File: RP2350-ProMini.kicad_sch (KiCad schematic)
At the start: 44 parts, among them J1 CONN_L, J2 CONN_U, J3 CONN_R2, J4 CONN_R, J5 CONN_R3, J6 USB_B_Micro, J7 CONN_JTAG, Q1 AO3400A, U1 W25Q128JVS, U2 RP2350A-QFN60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

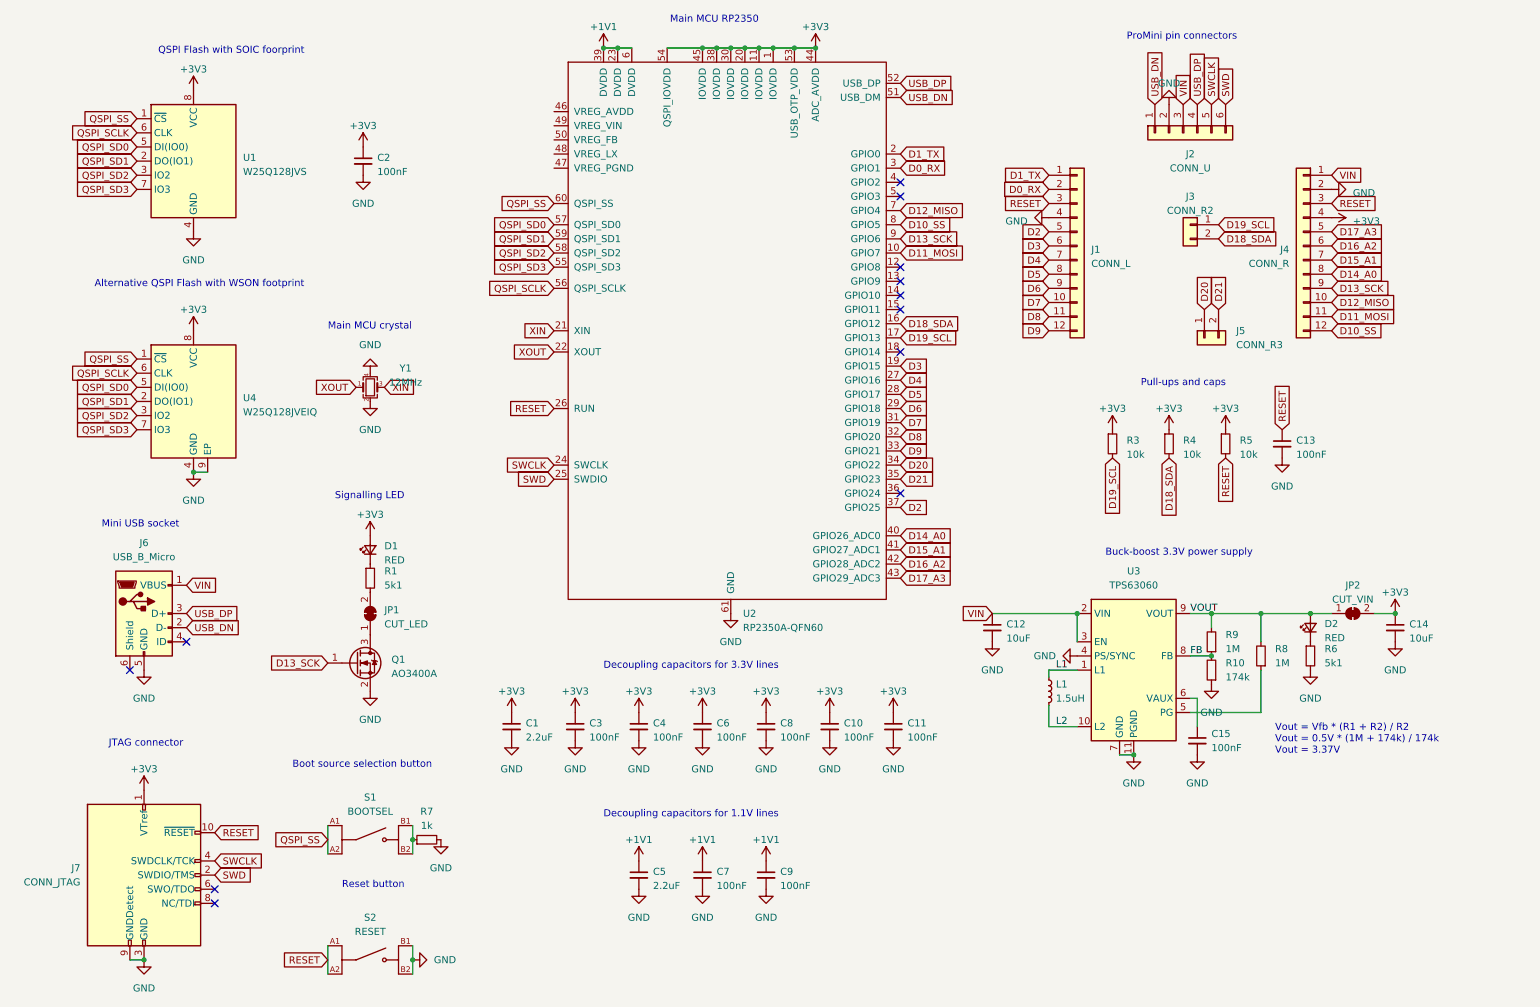
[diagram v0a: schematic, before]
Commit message: Added some routing
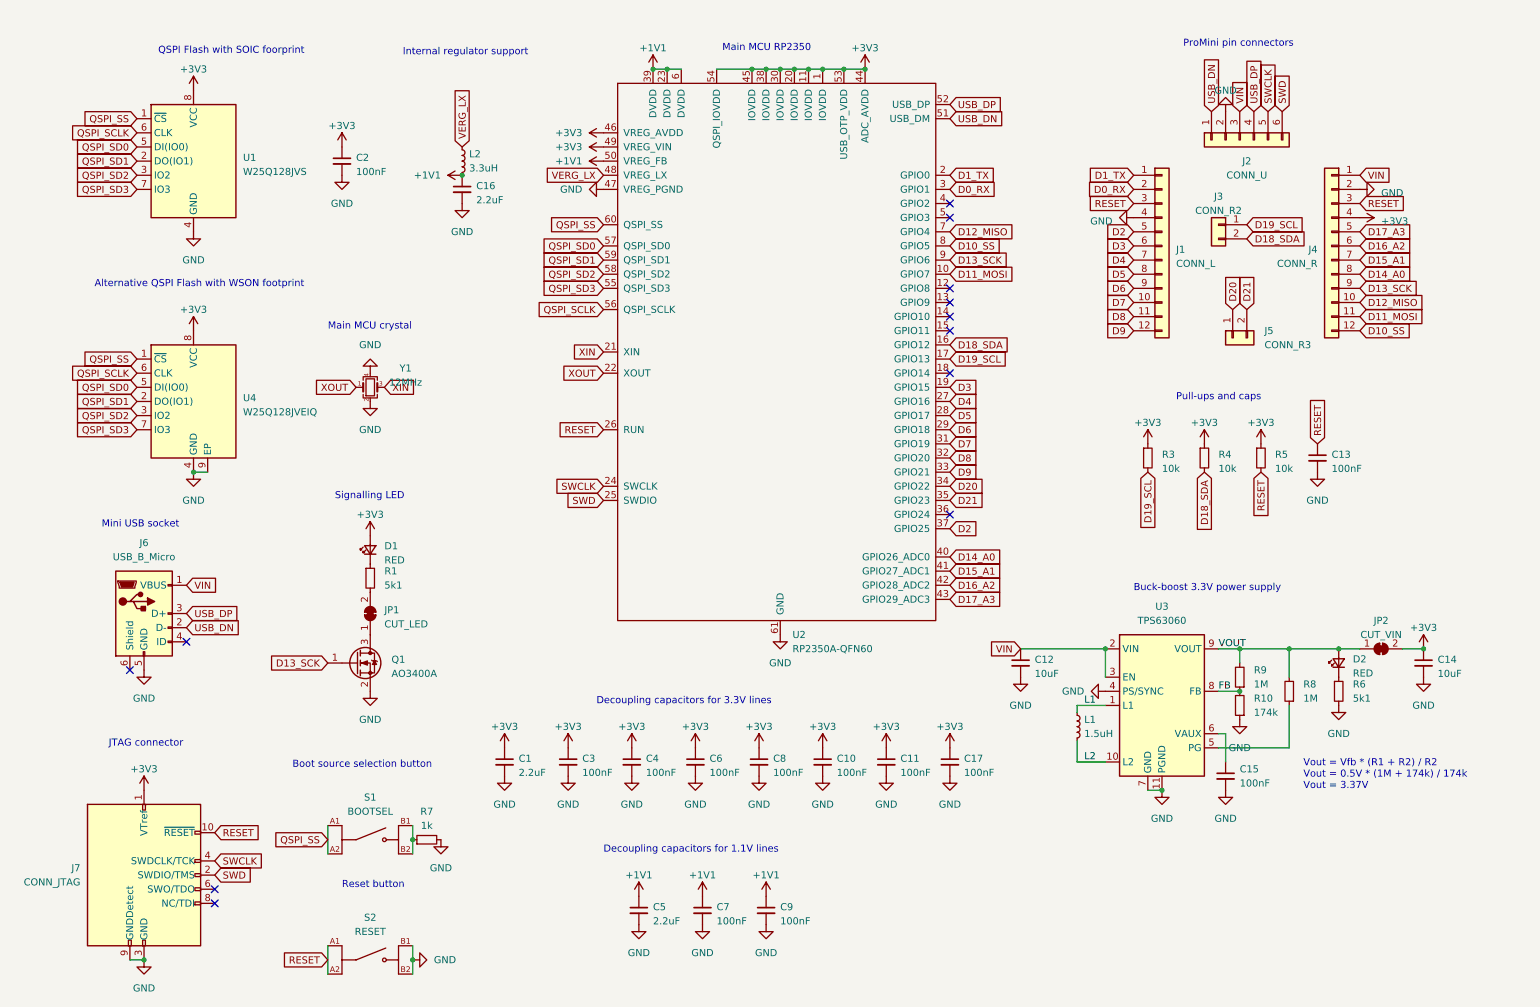
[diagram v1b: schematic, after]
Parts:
- added C16: 2.2uF, Capacitor_SMD:C_0603_1608Metric, symbol Device:C_Small
- added C17: 100nF, Capacitor_SMD:C_0402_1005Metric, symbol Device:C_Small
- added L2: 3.3uH, Inductor_SMD:L_0603_1608Metric, symbol Device:L_Small
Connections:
- net +1V1: now also U2.50 (VREG_FB), C16.1, L2.2
- net +3V3: now also U2.46 (VREG_AVDD), U2.49 (VREG_VIN), C17.1
- net GND: now also U2.47 (VREG_PGND), C16.2, C17.2
- net VERG_LX: now reaches U2.48 (VREG_LX)
- net VERG_LX: now also L2.1
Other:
- note added: "Internal regulator support"
- moved on the sheet: C1, C10, C11, C12, C13, C14, C15, C2, C3, C4, C5, C6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

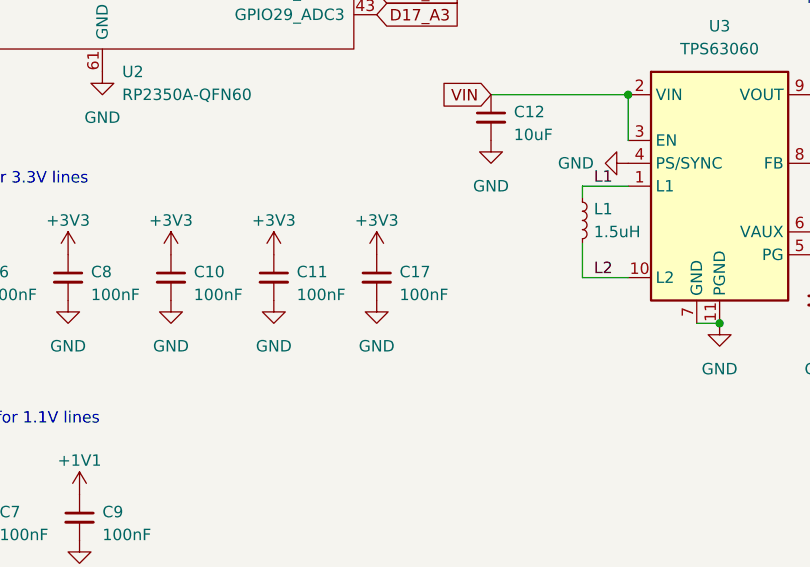
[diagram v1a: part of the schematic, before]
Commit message: Moved staff around.
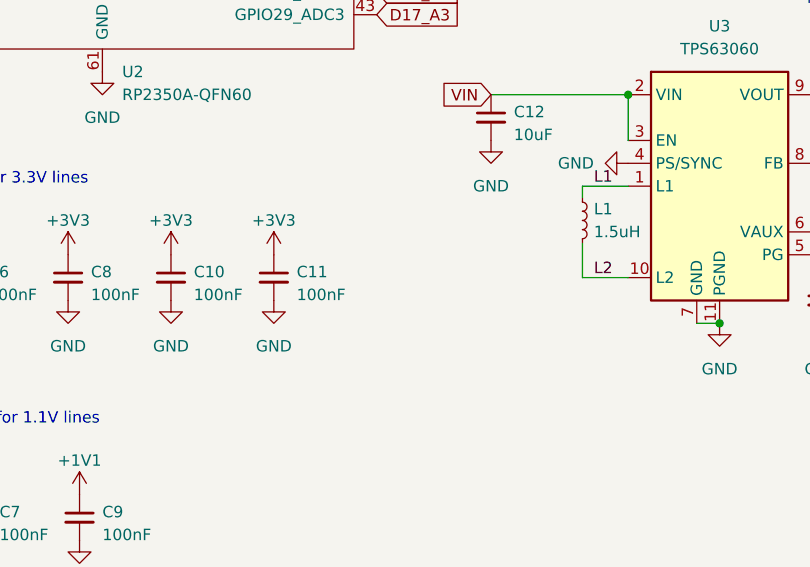
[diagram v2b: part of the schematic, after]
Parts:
- removed C17: 100nF, Capacitor_SMD:C_0402_1005Metric, symbol Device:C_Small
- C1, C16, C5: footprint Capacitor_SMD:C_0603_1608Metric -> Capacitor_SMD:C_0402_1005Metric
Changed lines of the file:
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@@
 	(title_block
 		(title "RP2350-ProMini-0010")
-		(date "2024-09-01")
+		(date "2024-09-03")
 		(rev "1.0")
 		(company "(c) 2024 Andriy Golovnya")
@@
 	)
 	(symbol
-		(lib_id "power:GND")
-		(at 185.42 154.94 0)
-		(unit 1)
-		(exclude_from_sim no)
-		(in_bom yes)
-		(on_board yes)
-		(dnp no)
-		(fields_autoplaced yes)
-		(property "Reference" "#PWR062"
-			(at 185.42 161.29 0)
-			(effects
-				(font
-					(size 1.27 1.27)
-				)
-				(hide yes)
-			)
-		)
-		(property "Value" "GND"
-			(at 185.42 160.02 0)
-			(effects
-				(font
-					(size 1.27 1.27)
-				)
-			)
-		)
-		(property "Footprint" ""
-			(at 185.42 154.94 0)
-			(effects
-				(font
-					(size 1.27 1.27)
-				)
-				(hide yes)
-			)
-		)
-		(property "Datasheet" ""
-			(at 185.42 154.94 0)
-			(effects
-				(font
-					(size 1.27 1.27)
-				)
-				(hide yes)
-			)
-		)
-		(property "Description" ""
-			(at 185.42 154.94 0)
-			(effects
-				(font
-					(size 1.27 1.27)
-				)
-				(hide yes)
-			)
-		)
-		(pin "1"
-		)
-		(instances
-			(project "RP2350-ProMini"
-				(path "/9a38a81c-7302-494f-9784-2ab4342a0a1d"
-					(reference "#PWR062")
-					(unit 1)
-				)
-			)
-		)
-	)
-	(symbol
-		(lib_id "Device:C_Small")
-		(at 185.42 152.4 0)
-		(unit 1)
-		(exclude_from_sim no)
-		(in_bom yes)
-		(on_board yes)
-		(dnp no)
-		(fields_autoplaced yes)
-		(property "Reference" "C17"
-			(at 187.96 151.7713 0)
-			(effects
-				(font
-					(size 1.27 1.27)
-				)
-				(justify left)
-			)
-		)
-		(property "Value" "100nF"
-			(at 187.96 154.3113 0)
-			(effects
-				(font
-					(size 1.27 1.27)
-				)
-				(justify left)
-			)
-		)
-		(property "Footprint" "Capacitor_SMD:C_0402_1005Metric"
-			(at 185.42 152.4 0)
-			(effects
-				(font
-					(size 1.27 1.27)
-				)
-				(hide yes)
-			)
-		)
-		(property "Datasheet" "~"
-			(at 185.42 152.4 0)
-			(effects
-				(font
-					(size 1.27 1.27)
-				)
-				(hide yes)
-			)
-		)
-		(property "Description" ""
-			(at 185.42 152.4 0)
-			(effects
-				(font
-					(size 1.27 1.27)
-				)
-				(hide yes)
-			)
-		)
-		(pin "1"
-		)
-		(pin "2"
-		)
-		(instances
-			(project "RP2350-ProMini"
-				(path "/9a38a81c-7302-494f-9784-2ab4342a0a1d"
-					(reference "C17")
-					(unit 1)
-				)
-			)
-		)
-	)
-	(symbol
 		(lib_id "power:+3V3")
 		(at 173.99 149.86 0)
@@
 	)
 	(symbol
-		(lib_id "power:+3V3")
-		(at 185.42 149.86 0)
-		(unit 1)
-		(exclude_from_sim no)
-		(in_bom yes)
-		(on_board yes)
-		(dnp no)
-		(fields_autoplaced yes)
-		(property "Reference" "#PWR061"
-			(at 185.42 153.67 0)
-			(effects
-				(font
-					(size 1.27 1.27)
-				)
-				(hide yes)
-			)
-		)
-		(property "Value" "+3V3"
-			(at 185.42 146.05 0)
-			(effects
-				(font
-					(size 1.27 1.27)
-				)
-			)
-		)
-		(property "Footprint" ""
-			(at 185.42 149.86 0)
-			(effects
-				(font
-					(size 1.27 1.27)
-				)
-				(hide yes)
-			)
-		)
-		(property "Datasheet" ""
-			(at 185.42 149.86 0)
-			(effects
-				(font
-					(size 1.27 1.27)
-				)
-				(hide yes)
-			)
-		)
-		(property "Description" ""
-			(at 185.42 149.86 0)
-			(effects
-				(font
-					(size 1.27 1.27)
-				)
-				(hide yes)
-			)
-		)
-		(pin "1"
-		)
-		(instances
-			(project "RP2350-ProMini"
-				(path "/9a38a81c-7302-494f-9784-2ab4342a0a1d"
-					(reference "#PWR061")
-					(unit 1)
-				)
-			)
-		)
-	)
-	(symbol
 		(lib_id "Device:C_Small")
 		(at 129.54 179.07 0)
@@
 			)
 		)
-		(property "Footprint" "Capacitor_SMD:C_0603_1608Metric"
+		(property "Footprint" "Capacitor_SMD:C_0402_1005Metric"
 			(at 129.54 179.07 0)
 			(effects
@@
 			)
 		)
-		(property "Footprint" "Capacitor_SMD:C_0603_1608Metric"
+		(property "Footprint" "Capacitor_SMD:C_0402_1005Metric"
 			(at 105.41 152.4 0)
 			(effects
@@
 			)
 		)
-		(property "Footprint" "Capacitor_SMD:C_0603_1608Metric"
+		(property "Footprint" "Capacitor_SMD:C_0402_1005Metric"
 			(at 97.79 49.53 0)
 			(effects
